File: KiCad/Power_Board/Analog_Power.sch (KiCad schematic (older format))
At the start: 10 parts

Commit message: Updated power board schematic.
Initial schematic draft. Probably will be modified once layout is
started.
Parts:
- removed U?: TPS63030, symbol TPS63030
- removed U? (x4): CS30, symbol CS30
- removed U?: LT8570, symbol LT8570
- added C? (x7): 10uF, symbol C_Small
- added C?: 0.1uF, symbol C_Small
- added C? (x2): 1nF, symbol C_Small
- added C? (x2): 47nF, symbol C_Small
- added C? (x5): 1uF, symbol C_Small
- added C? (x3): 2.2uF, symbol C_Small
- added C?: 47uF, symbol C_Small
- added C?: 20pF, symbol C_Small
- added D? (x2): DFLS240, symbol D_Schottky_Small
- added D?: 1N5261, symbol D_Schottky_Small
- added D?: 1N4148, symbol D_Small
- added L? (x2): 3.3uH, symbol INDUCTOR_SMALL
- added L?: 6.8uH, symbol INDUCTOR_SMALL
- added L?: 47uH, symbol INDUCTOR_SMALL
- added P? (x3): CONN_02X01, symbol CONN_02X01
- added Q?: IRLL024NQ, symbol Q_NMOS_GDSD
- added R?: 1.8M, symbol R_Small
- added R?: 180k, symbol R_Small
- added R? (x2): 0, symbol R_Small
- added R?: 5.6k, symbol R_Small
- added R?: 12k, symbol R_Small
- added R?: 2.15M, symbol R_Small
- added R?: 113k, symbol R_Small
- added R?: 100k, symbol R_Small
- added R?: 2.1M, symbol R_Small
- added R?: 20k, symbol R_Small
- added R?: 1k, symbol R_Small
- added R?: 10k, symbol R_Small
- added R?: 52.3k, symbol R_Small
- added R?: 5.9k, symbol R_Small
- added R?: 59k, symbol R_Small
- added R?: 50k, symbol R_Small
- added R?: 300k, symbol R_Small
- added TP? (x4): Test_Point, symbol Test_Point
- added U?: TPS63030, symbol TPS63030
- added U?: MAX152x, symbol MAX152x
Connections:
- net labels added: -15Va, 15Va, 5.5V, 50Va, 5Va, GND, Gnd, Vin
- wire segments 0 -> 152
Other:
- moved on the sheet: U?

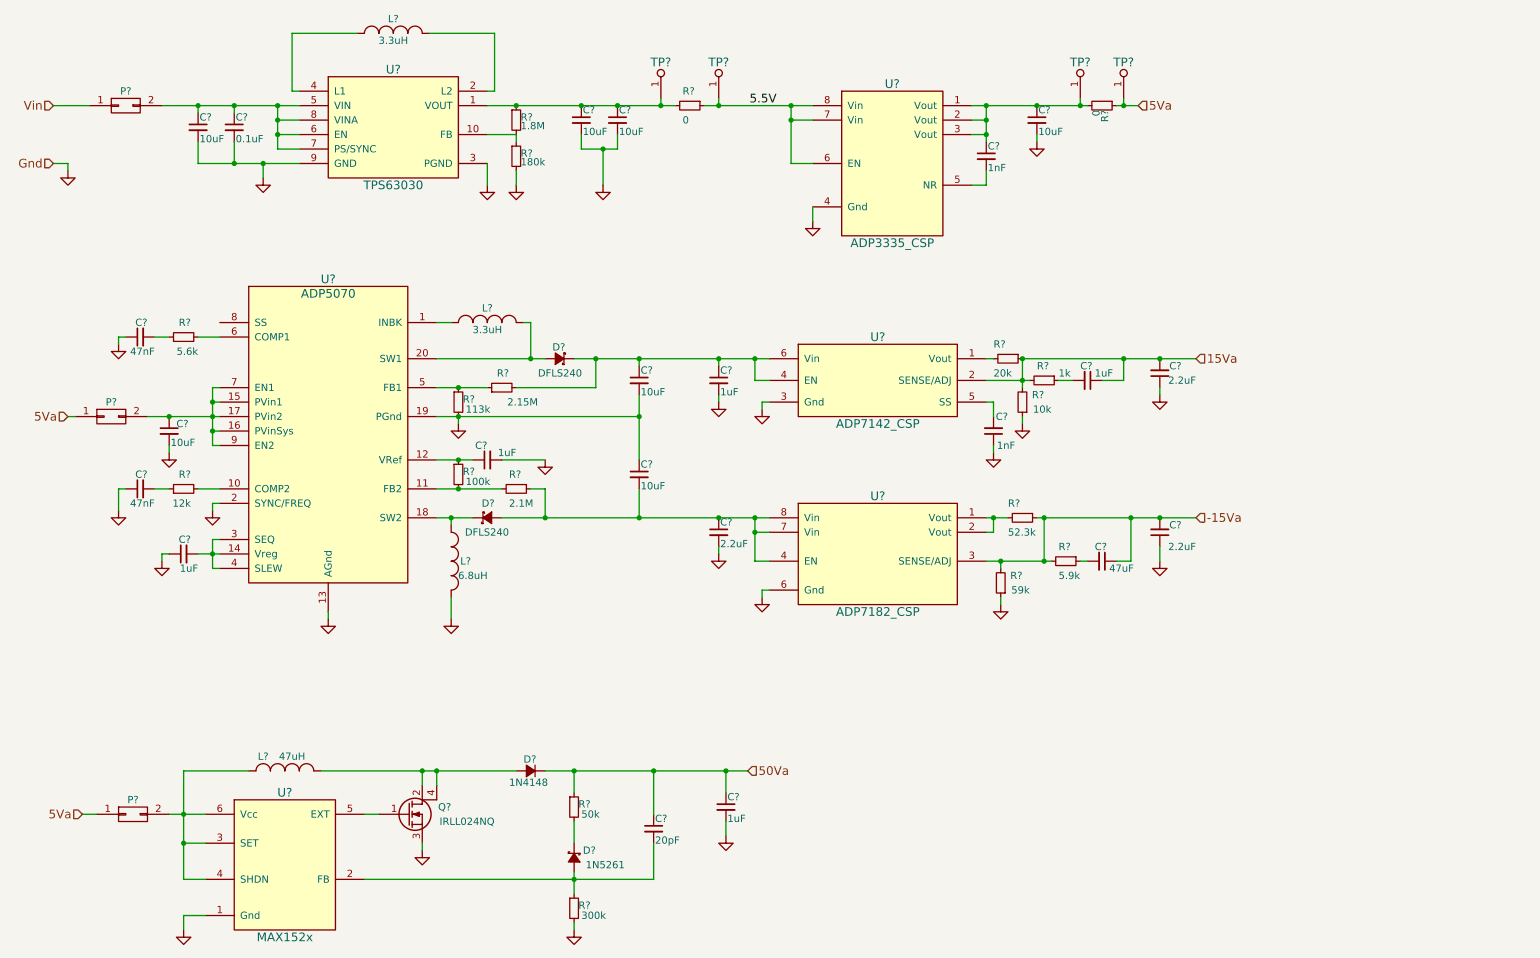
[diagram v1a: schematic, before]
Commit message: Power board fixes & Updated BOM
Initialized refdes.

Added test clip test points to all power lines (except DACs).

Fixed a feedback resistor mess up on the +/-15V LDOs.
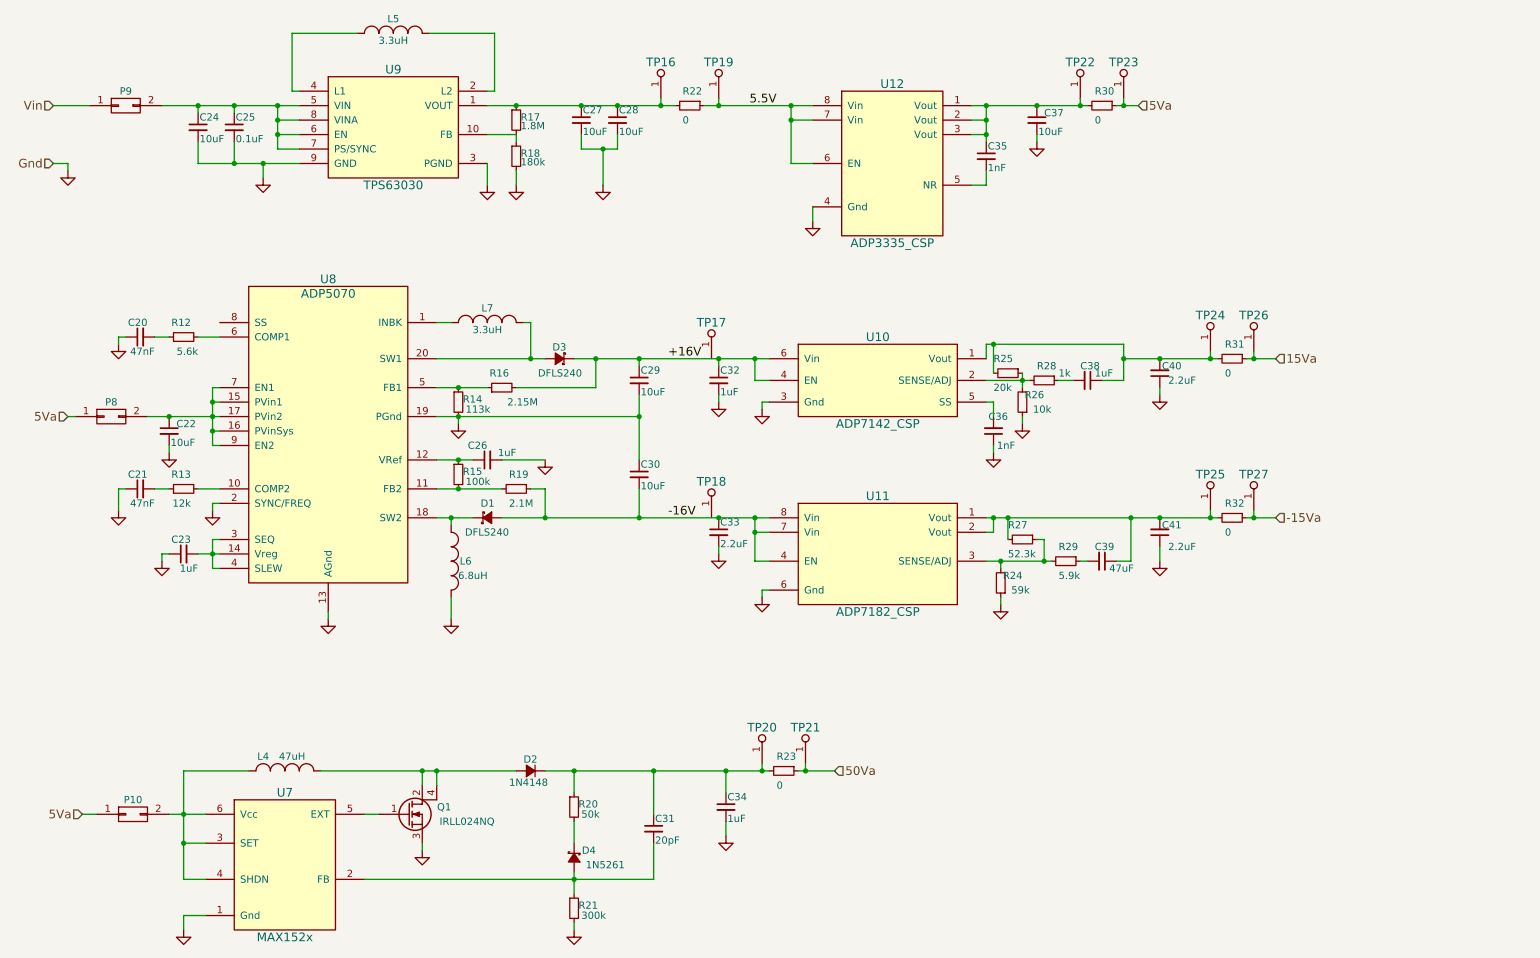
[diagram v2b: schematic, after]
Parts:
- added R23, R31, R32: 0, symbol R_Small
- added TP17, TP18, TP20, TP21, TP24, TP25, TP26, TP27: Test_Point, symbol Test_Point
- gave numbers to parts that had none: 62
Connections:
- net -15Va: now also R32.1, TP27.1; no longer C39.1, C41.2, R24.2, R27.1, R29.2, U11.3 (SENSE/ADJ)
- net 15Va: now also R31.1, TP26.1; no longer C38.1, C40.2, R25.1, R26.2, R28.2, U10.2 (SENSE/ADJ)
- net 50Va: now also R23.1, TP21.1; no longer C31.1, C34.1, D2.2 (C), R20.1
- net at R25.2, U10.1 (Vout): now also C38.1, C40.2, R31.2, TP24.1
- net +16V: now reaches C29.1, C32.1, D3.2 (C), R16.2, U10.4 (EN), U10.6 (Vin)
- net at R27.2, U11.1 (Vout), U11.2 (Vout): now also C39.1, C41.2, R32.2, TP25.1
- net -16V: now reaches C30.2, C33.1, D1.1 (A), R19.1, U11.4 (EN), U11.7 (Vin), U11.8 (Vin)
- new net: R25.1, R26.2, R28.2, U10.2 (SENSE/ADJ)
- new net: R24.2, R27.1, R29.2, U11.3 (SENSE/ADJ)
- new net: C31.1, C34.1, D2.2 (C), R20.1, R23.2, TP20.1
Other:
- moved on the sheet: R25, R27

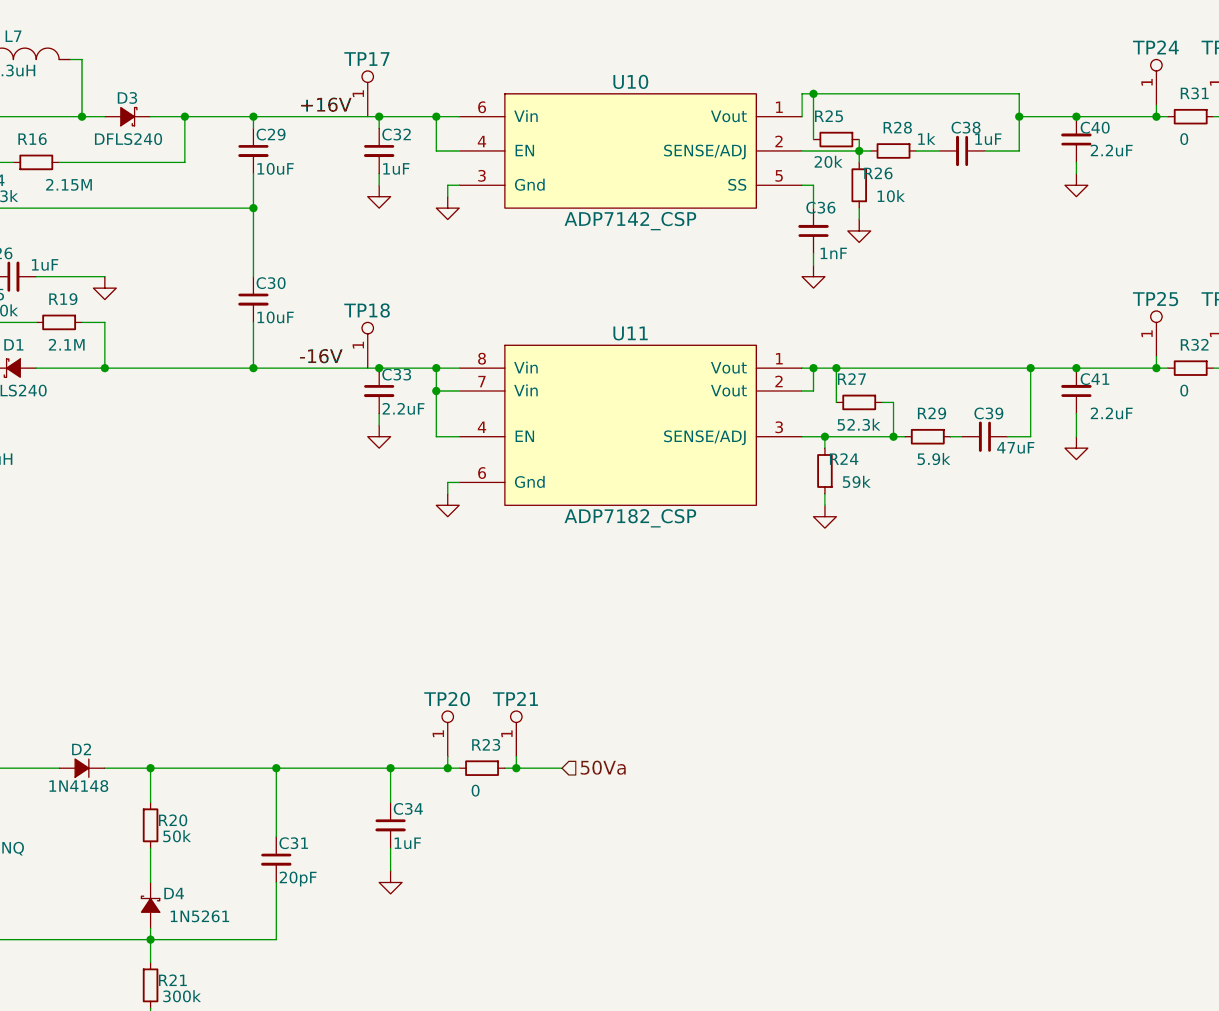
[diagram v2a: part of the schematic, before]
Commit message: Fixed -15V LDO & Updated BOM
-15V LDO had incorrect feedback resistors. +15V LDO seemed ok.

BOM updated to all tentatively selected parts.
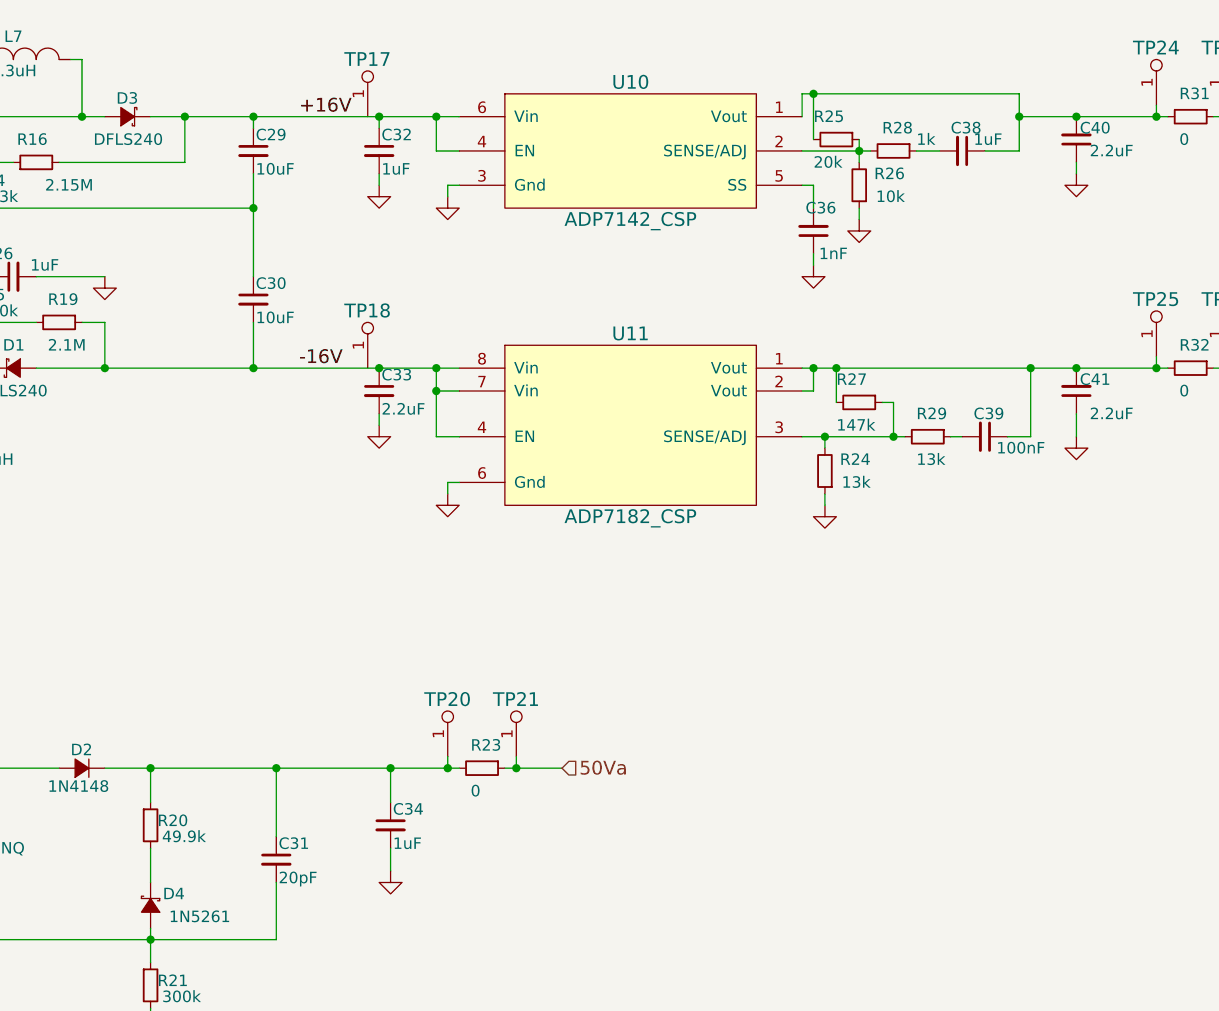
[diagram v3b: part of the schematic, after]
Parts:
- C39: value 47uF -> 100nF
- R20: value 50k -> 49.9k
- R24: value 59k -> 13k
- R27: value 52.3k -> 147k
- R29: value 5.9k -> 13k
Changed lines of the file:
@@
 U 1 1 5591F07A
 P 7500 3350
-F 0 "R26" H 7350 3300 50  0000 L CNN
+F 0 "R26" H 7300 3300 50  0000 L CNN
 F 1 "10k" H 7300 3400 50  0000 L CNN
 F 2 "" H 7500 3350 60  0000 C CNN
@@
 P 7500 4300
 F 0 "R27" V 7400 4200 50  0000 L CNN
-F 1 "52.3k" V 7600 4200 50  0000 L CNN
+F 1 "147k" V 7600 4200 50  0000 L CNN
 F 2 "" H 7500 4300 60  0000 C CNN
 F 3 "" H 7500 4300 60  0000 C CNN
@@
 P 7800 4450
 F 0 "R29" V 7700 4400 50  0000 L CNN
-F 1 "5.9k" V 7900 4400 50  0000 L CNN
+F 1 "13k" V 7900 4400 50  0000 L CNN
 F 2 "" H 7800 4450 60  0000 C CNN
 F 3 "" H 7800 4450 60  0000 C CNN
@@
 P 8050 4450
 F 0 "C39" V 7950 4400 50  0000 L CNN
-F 1 "47uF" V 8100 4500 50  0000 L CNN
+F 1 "100nF" V 8100 4500 50  0000 L CNN
 F 2 "" H 8050 4450 60  0000 C CNN
 F 3 "" H 8050 4450 60  0000 C CNN
@@
 U 1 1 55922B33
 P 7350 4600
-F 0 "R24" H 7200 4550 50  0000 L CNN
-F 1 "59k" H 7150 4650 50  0000 L CNN
+F 0 "R24" H 7150 4550 50  0000 L CNN
+F 1 "13k" H 7150 4650 50  0000 L CNN
 F 2 "" H 7350 4600 60  0000 C CNN
 F 3 "" H 7350 4600 60  0000 C CNN
@@
 P 4400 6150
 F 0 "R20" H 4430 6170 50  0000 L CNN
-F 1 "50k" H 4450 6100 50  0000 L CNN
+F 1 "49.9k" H 4450 6100 50  0000 L CNN
 F 2 "" H 4400 6150 60  0000 C CNN
 F 3 "" H 4400 6150 60  0000 C CNN

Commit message: Linked footprints to schematic.
Also cleaned up some footprint errors:
Changed IC footprint names to be invisible on the silkscreen layer.
Fixed test points that were lacking pin numbers causing netlist
failures.
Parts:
- C20, C21, C35, C36: footprint (none) -> Capacitors_SMD:C_0402
- C22, C24, C27, C28, C29, C30, C37: footprint (none) -> Capacitors_SMD:C_1210
- C23, C25, C26, C31, C32, C38, C39: footprint (none) -> Capacitors_SMD:C_0603
- C33, C40, C41: footprint (none) -> Capacitors_SMD:C_0805
- C34: footprint (none) -> Capacitors_SMD:C_1206
- D1, D3: footprint (none) -> OpenCamera:DFLS240
- D2: footprint (none) -> OpenCamera:1N4148
- D4: footprint (none) -> Diodes_ThroughHole:Diode_DO-35_SOD27_Horizontal_RM10
- L4: footprint (none) -> OpenCamera:NS12555
- L5, L6, L7: footprint (none) -> OpenCamera:NRS5030
- P10, P8, P9: footprint (none) -> OpenCamera:SMD_JUMPER
- Q1: footprint (none) -> SMD_Packages:SOT-223
- R12, R13, R14, R15, R16, R17, R18, R19, R20, R21, R22, R23, R24, R25, R26, R27, R28, R29, R30, R31, R32: footprint (none) -> Resistors_SMD:R_0402
- TP16, TP17, TP18, TP19, TP20, TP21, TP22, TP23, TP24, TP25, TP26, TP27: footprint (none) -> OpenCamera:TEST_POINT_SMD
- U10: footprint (none) -> OpenCamera:ADP7142
- U11: footprint (none) -> OpenCamera:ADP7182
- U12: footprint (none) -> OpenCamera:ADP3335
- U7: footprint (none) -> OpenCamera:SOT_623
- U8: footprint (none) -> OpenCamera:ADP5070
- U9: footprint (none) -> OpenCamera:TPS63030

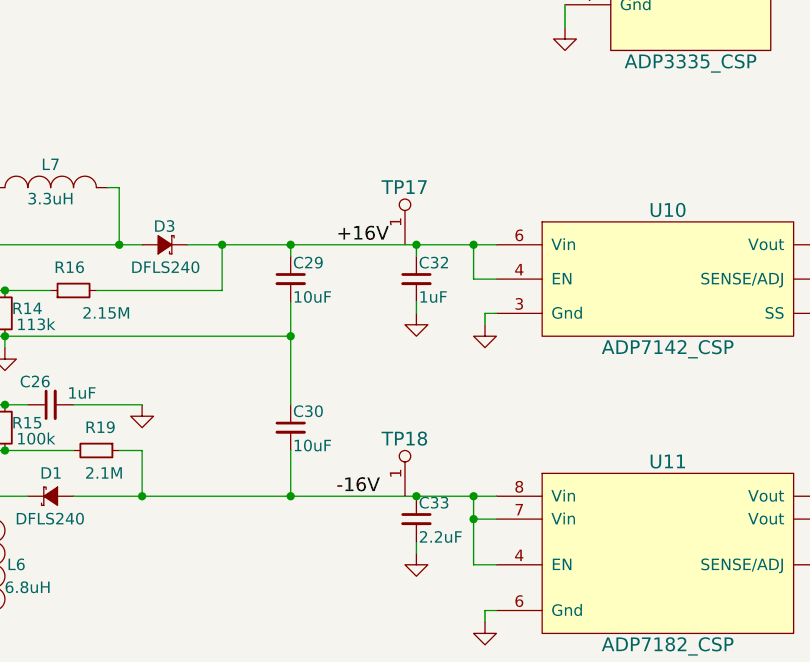
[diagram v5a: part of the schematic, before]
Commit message: Rough PCB component placement.
Organized parts by module and roughly placed them in appropriate
locations on the board.

Also fixed a couple of test points that weren't properly connected to a
net.
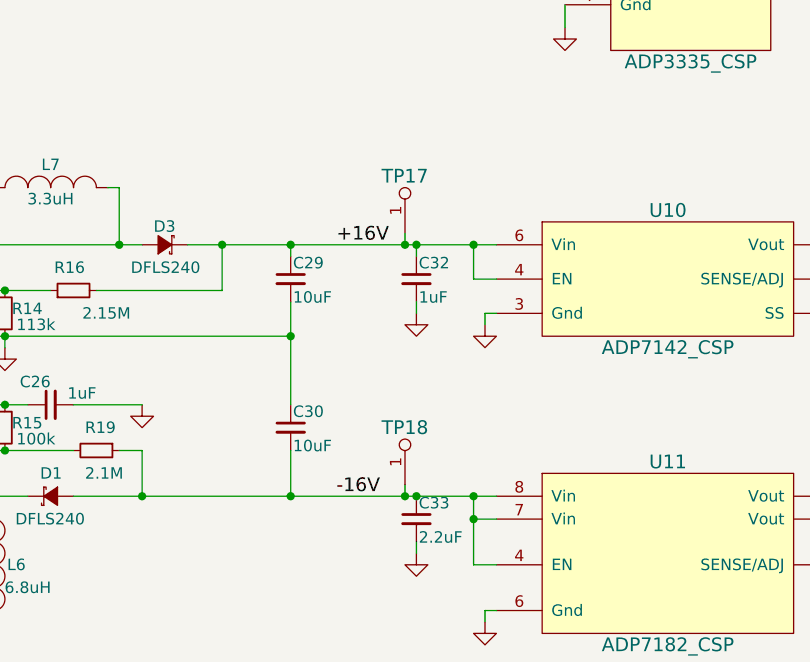
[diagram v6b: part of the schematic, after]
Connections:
- net +16V: now also TP17.1
- net -16V: now also TP18.1
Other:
- moved on the sheet: TP17, TP18
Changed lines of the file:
@@
 L Test_Point TP17
 U 1 1 558FA43E
-P 5350 3050
-F 0 "TP17" H 5350 3300 60  0000 C CNN
-F 1 "Test_Point" H 5350 3400 60  0001 C CNN
-F 2 "OpenCamera:TEST_POINT_SMD" H 5350 3050 60  0001 C CNN
-F 3 "" H 5350 3050 60  0000 C CNN
-	1    5350 3050
+P 5350 3000
+F 0 "TP17" H 5350 3250 60  0000 C CNN
+F 1 "Test_Point" H 5350 3350 60  0001 C CNN
+F 2 "OpenCamera:TEST_POINT_SMD" H 5350 3000 60  0001 C CNN
+F 3 "" H 5350 3000 60  0000 C CNN
+	1    5350 3000
 	1    0    0    -1
 $EndComp
@@
 L Test_Point TP18
 U 1 1 558FAA1B
-P 5350 4150
-F 0 "TP18" H 5350 4400 60  0000 C CNN
-F 1 "Test_Point" H 5350 4500 60  0001 C CNN
-F 2 "OpenCamera:TEST_POINT_SMD" H 5350 4150 60  0001 C CNN
-F 3 "" H 5350 4150 60  0000 C CNN
-	1    5350 4150
+P 5350 4100
+F 0 "TP18" H 5350 4350 60  0000 C CNN
+F 1 "Test_Point" H 5350 4450 60  0001 C CNN
+F 2 "OpenCamera:TEST_POINT_SMD" H 5350 4100 60  0001 C CNN
+F 3 "" H 5350 4100 60  0000 C CNN
+	1    5350 4100
 	1    0    0    -1
 $EndComp
@@
 	7500 3150 7500 3250
 Connection ~ 7500 3200
+Wire Wire Line
+	5350 3000 5350 3050
+Connection ~ 5350 3050
+Wire Wire Line
+	5350 4100 5350 4150
+Connection ~ 5350 4150
 $EndSCHEMATC
